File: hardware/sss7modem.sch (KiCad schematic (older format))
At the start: 14 parts, among them IC1 MCP2551-I/SN, K1 CONN_3, P1 CONN_4

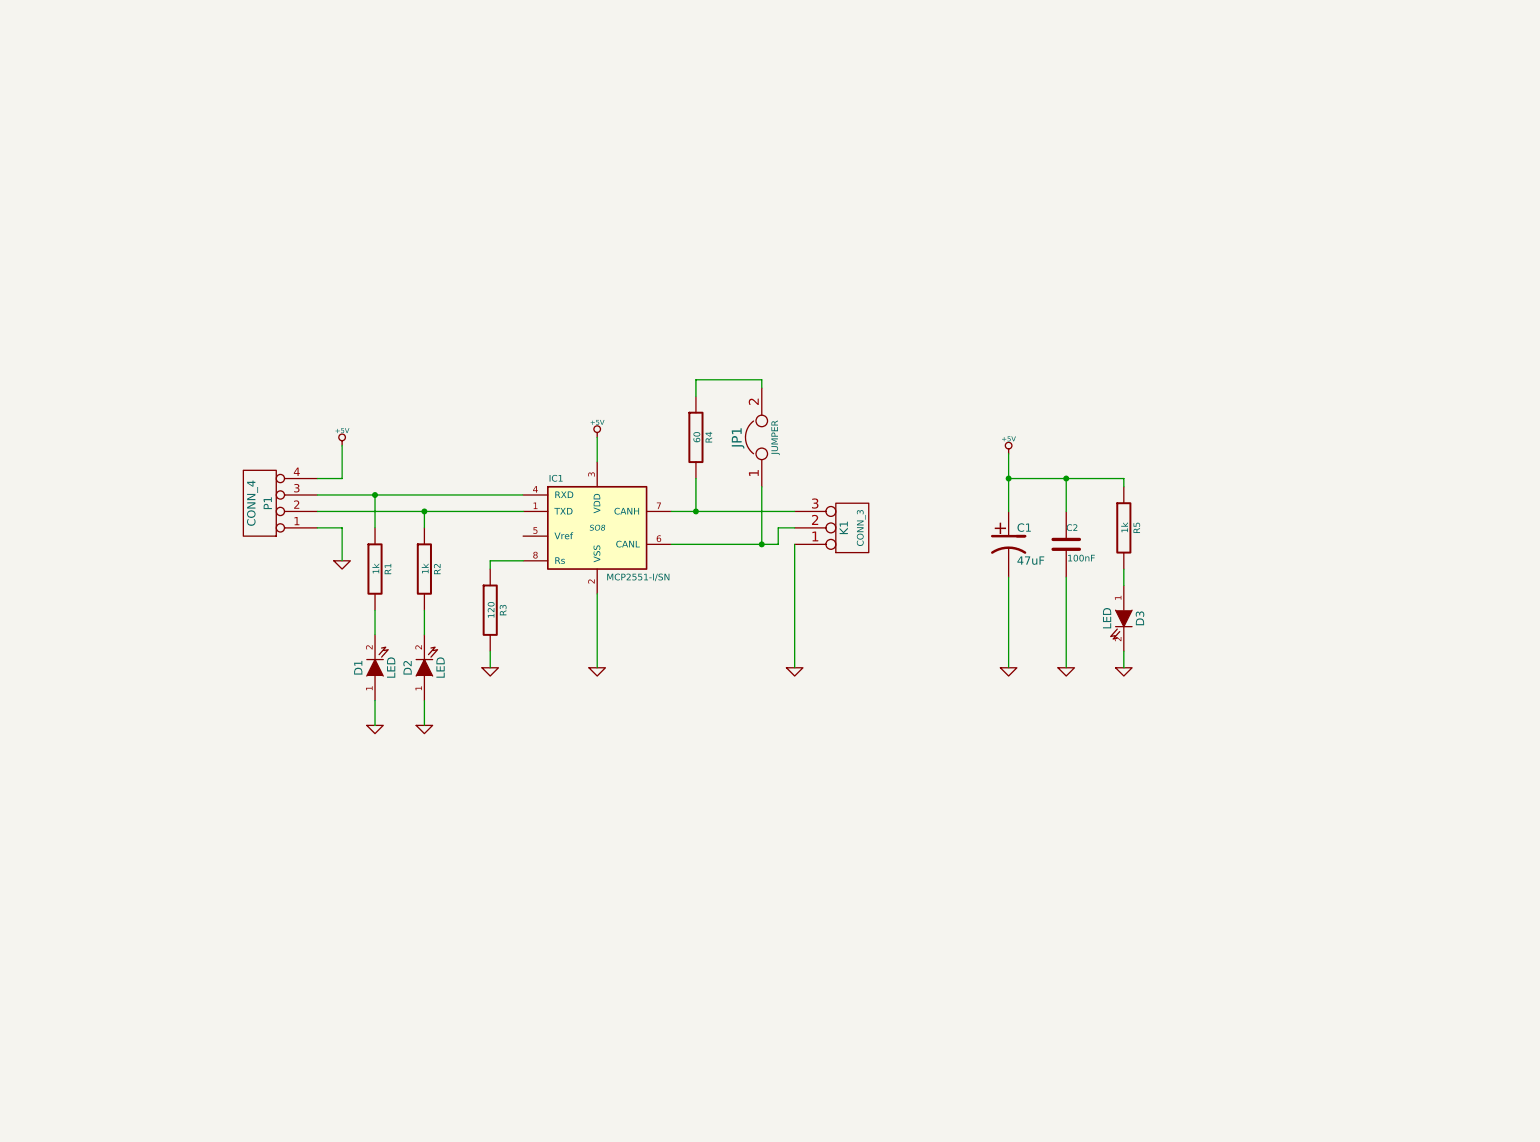
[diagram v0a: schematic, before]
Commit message: Changed schematic for floating common on bus side
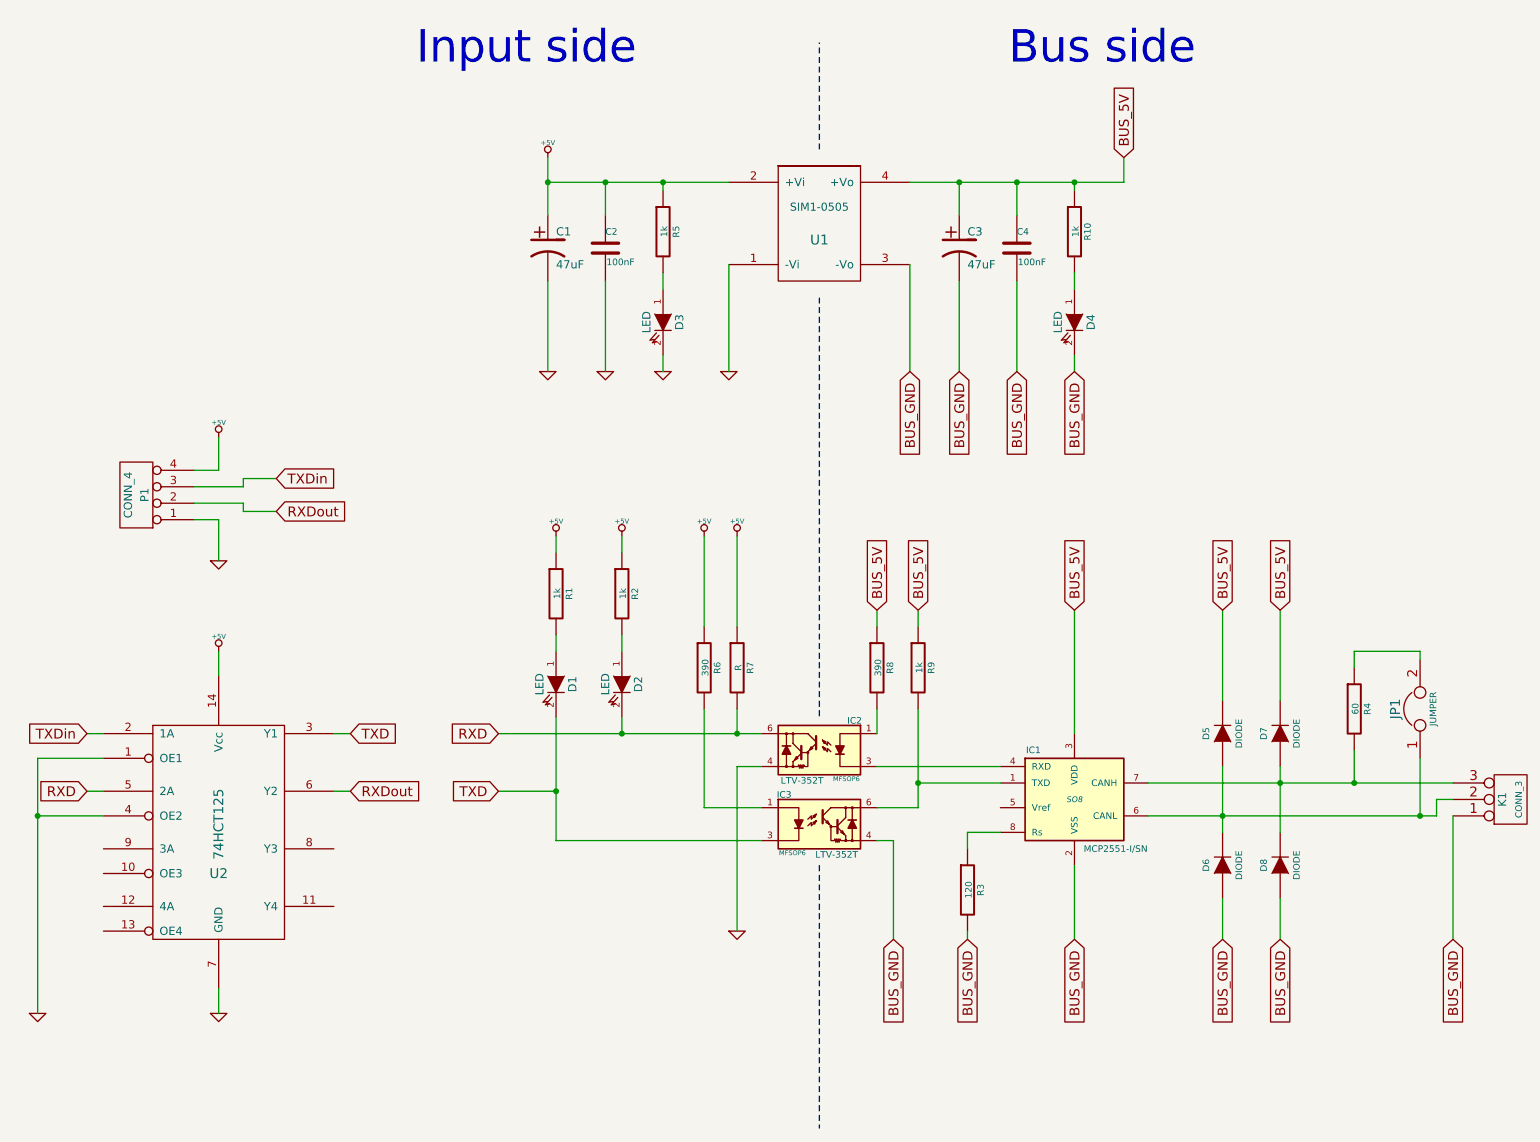
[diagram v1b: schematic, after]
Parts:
- added C3: 47uF, ~, symbol CP1
- added C4: 100nF, ~, symbol C
- added D4: LED, ~, symbol LED
- added D5, D6, D7, D8: DIODE, ~, symbol DIODE
- added IC2, IC3: LTV-352T, MFSOP6, symbol LTV-352T
- added R10, R9: 1k, ~, symbol R
- added R6, R8: 390, ~, symbol R
- added R7: R, ~, symbol R
- added U1: SIM1-0505, ~, symbol DCDC
- added U2: 74HCT125, ~, symbol 74HCT125
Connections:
- net +5V: now also R1.1, R2.1, R6.1, R7.1, U1.2 (+Vi), U2.14 (Vcc); no longer IC1.3 (VDD)
- net GND: now also IC2.4, U1.1 (-Vi), U2.1 (OE1), U2.4 (OE2), U2.7 (GND); no longer D1.1 (A), D2.1 (A), IC1.2 (VSS), K1.1 (P1), R3.2
- net at R2.2: now also D2.1 (A); no longer D2.2 (K)
- net at R1.2: now also D1.1 (A); no longer D1.2 (K)
- net at IC1.6 (CANL), JP1.1, K1.2 (PM): now also D5.1 (A), D6.2 (K)
- net at IC1.7 (CANH), K1.3 (P3), R4.2: now also D7.1 (A), D8.2 (K)
- new net: IC1.1 (TXD), IC3.6, R9.2
- new net: IC1.4 (RXD), IC2.3
- new net: IC3.1, R6.2
- new net: IC2.1, R8.2
- new net: D4.1 (A), R10.2
- new net BUS_5V: C3.1, C4.1, D5.2 (K), D7.2 (K), IC1.3 (VDD), R10.1, R8.1, R9.1, U1.4 (+Vo)
- new net BUS_GND: C3.2, C4.2, D4.2 (K), D6.1 (A), D8.1 (A), IC1.2 (VSS), IC3.4, K1.1 (P1), R3.2, U1.3 (-Vo)
- new net RXD: D2.2 (K), IC2.6, R7.2, U2.5 (2A)
- new net RXDout: P1.2 (P2), U2.6 (Y2)
- new net TXD: D1.2 (K), IC3.3, U2.3 (Y1)
- new net TXDin: P1.3 (P3), U2.2 (1A)
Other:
- note added: "Bus side"
- note added: "Input side"
- moved on the sheet: C1, C2, D1, D2, D3, IC1, JP1, K1, P1, R1, R2, R3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
